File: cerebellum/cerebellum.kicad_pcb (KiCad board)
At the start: 4 copper layers, 91.5 x 52 mm, 89 parts, among them J1 Power_IN, J10 Arm_R, J11 Light, J2 Power_Back, J3 GD_LINK, J4 GD_LINK, J5 Head, J7 Leg_L, J8 Leg_R, J9 Arm_L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

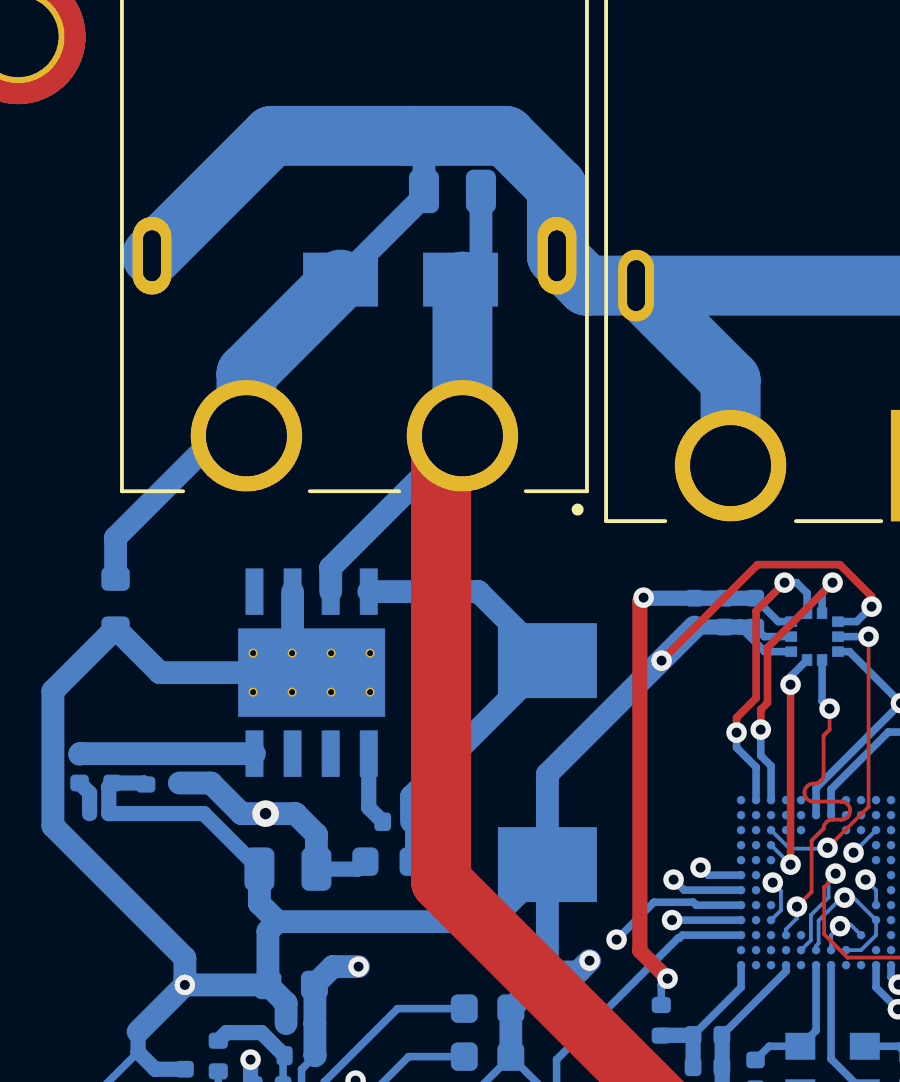
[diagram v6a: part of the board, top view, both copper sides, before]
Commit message: [Fix] Fix package of diode in cerebellum
Signed-off-by: Homalozoa <nx.tardis@gmail.com>
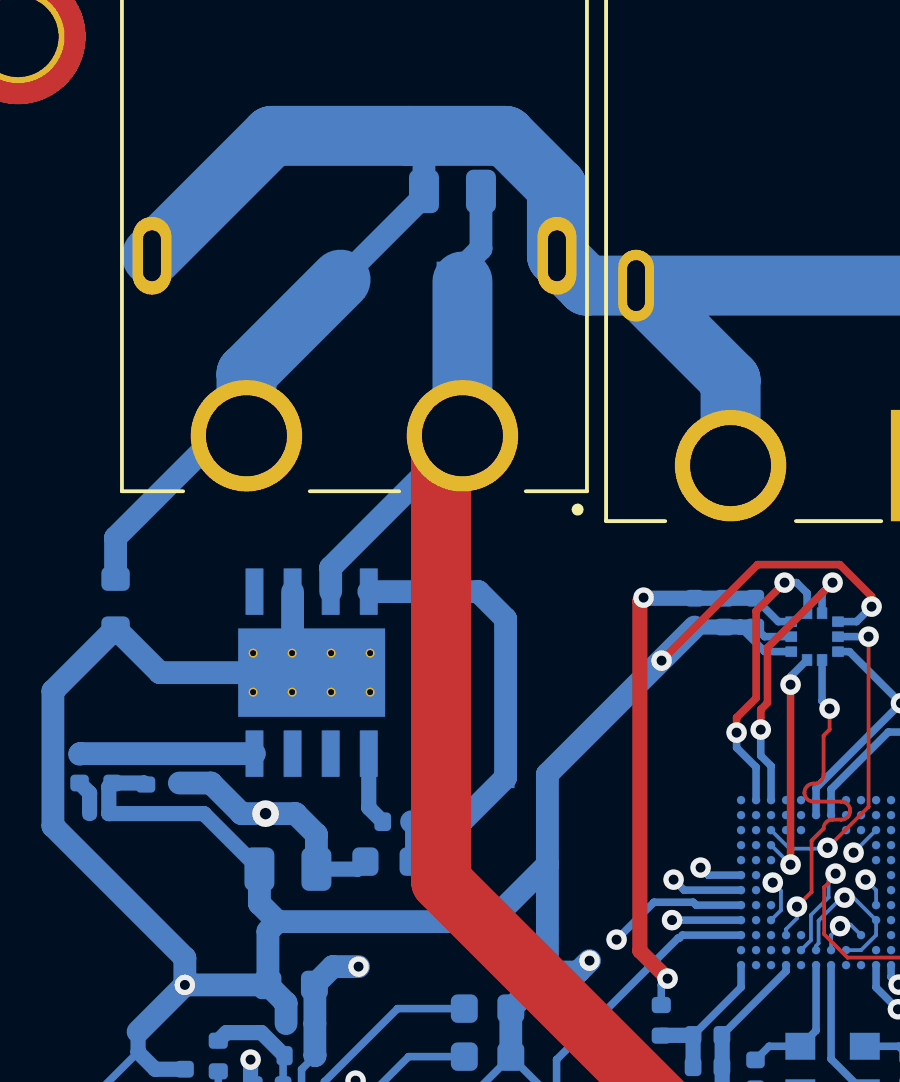
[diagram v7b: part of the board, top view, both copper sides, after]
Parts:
- D1: value 30V -> SMF30CA; footprint Diode_SMD:D_SMA -> Diode_SMD:D_SOD-123
- D2: value B340 -> ESD5Z3V3; footprint Diode_SMD:D_SMC -> Diode_SMD:D_SOD-523
- moved D2 0.86 mm to (123.6, 101.1), turned to 0 degrees

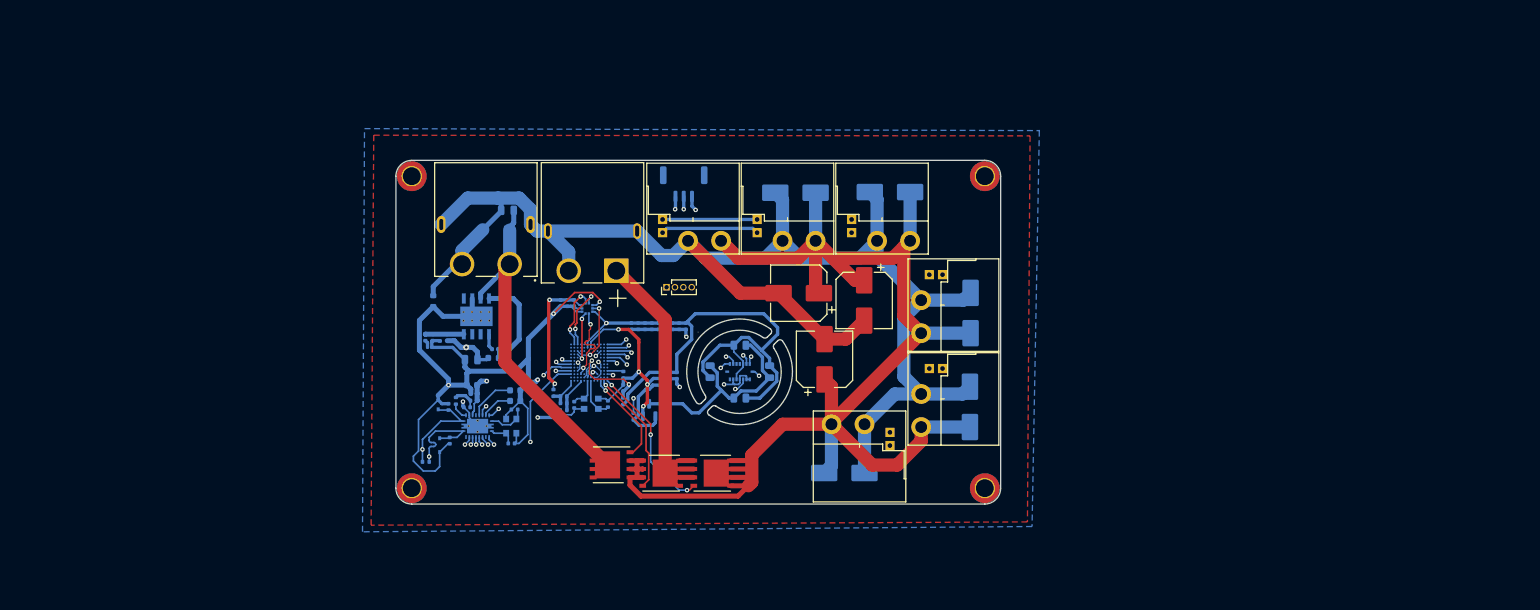
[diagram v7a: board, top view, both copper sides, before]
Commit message: [Modify] Refactor cerebellum for replacing xt30/60s
Signed-off-by: Homalozoa <nx.tardis@gmail.com>
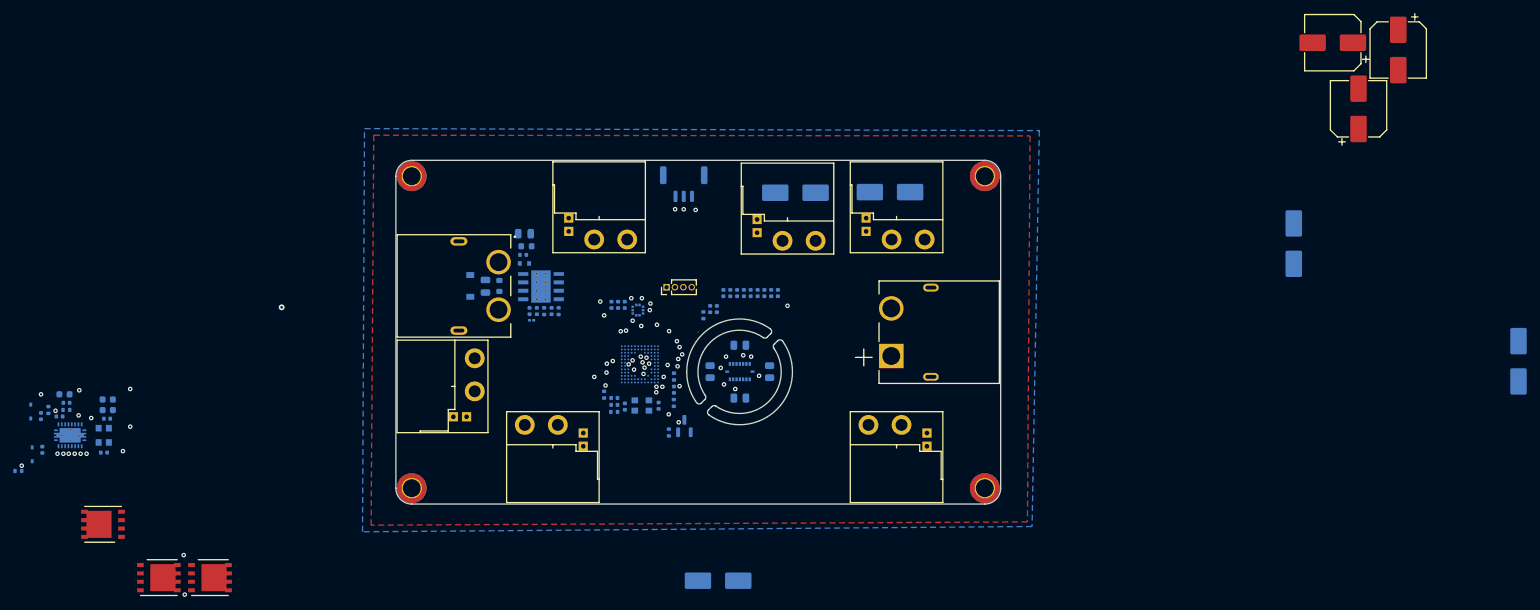
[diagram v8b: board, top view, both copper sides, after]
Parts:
- moved C36 89.2 mm to (246.0, 56.2)
- moved C38 89.2 mm to (255.9, 57.3)
- moved C40 89.2 mm to (249.9, 66.2)
- moved C35 83.3 mm to (274.1, 104.4)
- moved Q4 77.6 mm to (76.2, 137.3)
- moved Q3 77.6 mm to (68.5, 137.3)
- moved Q2 77.5 mm to (59.9, 128.9)
- moved C16 61.7 mm to (53.4, 112.8)
- moved C22 61.7 mm to (50.8, 117.8)
- moved C26 61.7 mm to (54.1, 109.4)
- moved D3 61.7 mm to (49.2, 118.5)
- moved D4 61.7 mm to (49.0, 112.0)
- moved C14 61.7 mm to (60.1, 118.2)
- moved C15 61.7 mm to (60.6, 113.1)
- moved C23 61.7 mm to (50.6, 112.7)
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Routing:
- net GND: track 253.0 -> 0.00 mm, vias 15 -> 12
- net GNDA: track 215.5 -> 0.00 mm
- net PWR_EXPORT: track 204.3 -> 0.00 mm
- net +3V3: track 182.6 -> 0.00 mm, vias 6 -> 5
- net CAN_L: track 167.0 -> 0.00 mm
- net CAN_H: track 166.4 -> 0.00 mm, vias 1 -> 0
- net +24V: track 78.3 -> 0.00 mm
- net BMI_SDO: track 48.7 -> 0.00 mm
- net BMI_SDI: track 42.8 -> 0.00 mm
- net EXT_PWR: track 40.1 -> 0.00 mm
- net TCAN_SDO: track 33.6 -> 0.00 mm
- net Net-(Q1-Pad3): track 33.2 -> 0.00 mm
- net SWCLK: track 32.8 -> 0.00 mm
- net ACC_SCS: track 30.3 -> 0.00 mm
- net BMI_SCK: track 29.7 -> 0.00 mm
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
